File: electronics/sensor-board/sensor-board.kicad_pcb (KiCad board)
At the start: 4 copper layers, 270 x 30 mm, 196 parts, among them J1 Load Cell Input, J10 Load Cell Input, J11 FSR Input, J12 Digital Input, J13 Conn_02x04_Odd_Even, J14 Conn_02x04_Odd_Even, J15 Conn_02x04_Odd_Even, J16 Conn_02x04_Odd_Even, J17 Conn_01x06_Male, J18 USB_C_Receptacle_USB2.0, J19 Conn_02x04_Odd_Even, J2 FSR Input, J20 Barrel_Jack_MountingPin, J3 Digital Input, J4 Load Cell Input, J5 FSR Input, J6 Digital Input, J7 Load Cell Input, J8 FSR Input, J9 Digital Input, SW1 SW_DIP_x02, SW10 SW_DIP_x02, SW11 SW_DIP_x02, SW12 SW_DIP_x02, SW2 SW_DIP_x02, SW3 SW_DIP_x02, SW4 SW_DIP_x02, SW5 SW_Push, SW6 SW_Push, SW7 SW_DIP_x02, SW8 SW_DIP_x02, SW9 SW_DIP_x02, U1 LMV321, U10 TJA1042T-3, U11 74HCT245, U12 AMS1117-3.3, U13 TPS5430DDA, U2 INA826, U3 LMV321, U4 INA826, U5 LMV321, U6 INA826, U7 LMV321, U8 INA826, U9 STM32F302C8Tx, Y1 8MHz

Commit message: Remove DIP switches and re-organize CAN connectors
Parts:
- removed C51, C52, C54, C56: 100u, Capacitor_SMD:C_1210_3225Metric
- removed C53: 1u, Capacitor_SMD:C_0603_1608Metric
- removed C55: 100n, Capacitor_SMD:C_0603_1608Metric
- removed H3, H4: MountingHole_Pad, MountingHole:MountingHole_3.2mm_M3_Pad
- removed J19: Conn_02x04_Odd_Even, Connector_PinHeader_2.54mm:PinHeader_2x04_P2.54mm_Vertical
- removed J20: Barrel_Jack_MountingPin, sensor-board:BarrelJack_MP
- removed R54, R55: 5.1k, Resistor_SMD:R_0603_1608Metric
- removed R56: 1.5k, Resistor_SMD:R_0603_1608Metric
- removed R57, R58: 22R, Resistor_SMD:R_0603_1608Metric
- removed R59, R60, R61, R62, R63, R64, R65, R66, R67: 10k, Resistor_SMD:R_0603_1608Metric
- removed R68: 3.3k, Resistor_SMD:R_0603_1608Metric
- removed SW10, SW11, SW12, SW3, SW4, SW7, SW8, SW9: SW_DIP_x02, Button_Switch_THT:SW_DIP_SPSTx02_Slide_6.7x6.64mm_W7.62mm_P2.54mm_LowProfile
- removed SW5, SW6: SW_Push, sensor-board:TS-1187A-B-A-B
- C40: value 100p -> 100n
- C41: value 4.7n -> 10u; footprint Capacitor_SMD:C_0603_1608Metric -> Capacitor_SMD:C_1206_3216Metric
- C42: value 100p -> 10u; footprint Capacitor_SMD:C_0603_1608Metric -> Capacitor_SMD:C_1206_3216Metric
- C43: value 100p -> 22u; footprint Capacitor_SMD:C_0603_1608Metric -> Capacitor_SMD:C_1206_3216Metric
- C44: value 4.7n -> 100n
- C45: value 100p -> 100u; footprint Capacitor_SMD:C_0603_1608Metric -> Capacitor_SMD:C_1210_3225Metric
- C46: value 100n -> 100u; footprint Capacitor_SMD:C_0603_1608Metric -> Capacitor_SMD:C_1210_3225Metric
- C47: value 10u -> 1u; footprint Capacitor_SMD:C_1206_3216Metric -> Capacitor_SMD:C_0603_1608Metric
- C48: value 10u -> 100u; footprint Capacitor_SMD:C_1206_3216Metric -> Capacitor_SMD:C_1210_3225Metric
- C49: value 22u -> 100u; footprint Capacitor_SMD:C_1206_3216Metric -> Capacitor_SMD:C_1210_3225Metric
- J15: value Conn_02x04_Odd_Even -> Conn_01x06_Male; footprint Connector_PinHeader_2.54mm:PinHeader_2x04_P2.54mm_Vertical -> Connector_PinHeader_2.54mm:PinHeader_1x06_P2.54mm_Vertical
- J16: value Conn_02x04_Odd_Even -> USB_C_Receptacle_USB2.0; footprint Connector_PinHeader_2.54mm:PinHeader_2x04_P2.54mm_Vertical -> Connector_USB:USB_C_Receptacle_Palconn_UTC16-G
- J17: value Conn_01x06_Male -> Conn_02x04_Odd_Even; footprint Connector_PinHeader_2.54mm:PinHeader_1x06_P2.54mm_Vertical -> Connector_PinHeader_2.54mm:PinHeader_2x04_P2.54mm_Vertical
- J18: value USB_C_Receptacle_USB2.0 -> Barrel_Jack_MountingPin; footprint Connector_USB:USB_C_Receptacle_Palconn_UTC16-G -> sensor-board:BarrelJack_MP
- R34: value 10k -> 47R
- R35: value 10k -> 56R
- R36: value 10k -> 120R
- R37: value 10k -> 220R
- R38, R39: value 10k -> 5.1k
- R40: value 10k -> 1.5k
- R41: value 10k -> 22R
- R42: value 47R -> 22R
- R43: value 56R -> 10k
- R44: value 120R -> 10k
- R45: value 220R -> 10k
- R46, R47, R50, R51: value 27R -> 10k
- R48, R49, R52: value 33R -> 10k
- R53: value 33R -> 3.3k
- SW1, SW2: value SW_DIP_x02 -> SW_Push; footprint Button_Switch_THT:SW_DIP_SPSTx02_Slide_6.7x6.64mm_W7.62mm_P2.54mm_LowProfile -> sensor-board:TS-1187A-B-A-B
- moved H2 209.3 mm to (315.8, 102.6)
- moved J14 202.2 mm to (315.9, 111.2)
- moved U13 183.7 mm to (334.2, 101.0)
- moved J15 143.6 mm to (207.4, 117.0), turned to 90 degrees
- moved SW1 142.5 mm to (216.2, 126.4)
- moved U9 142.4 mm to (212.4, 138.4), turned to 45 degrees
- moved J18 136.0 mm to (304.2, 106.6), turned to -90 degrees
- moved C35 127.7 mm to (219.2, 138.4), turned to -90 degrees
- moved SW2 124.9 mm to (208.6, 126.4)
- moved C31 124.7 mm to (218.4, 130.0)
- moved C33 121.9 mm to (212.4, 145.2)
- moved C36 112.8 mm to (212.4, 131.6)
- moved C37 105.7 mm to (205.6, 138.4), turned to 90 degrees
- moved R33 103.3 mm to (206.4, 130.0), turned to 180 degrees
- moved C49 93.5 mm to (231.3, 88.3)
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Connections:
- C3 pad 2: Net-(C10-Pad2) -> Net-(C3-Pad2)
- C38 pad 1: +3.3V -> GND
- C39 pad 1: GND -> +3.3V
- C4 pad 1: Net-(C10-Pad2) -> Net-(C3-Pad2)
- C4 pad 2: Net-(C11-Pad2) -> Net-(C4-Pad2)
- C40 pad 1: Net-(C40-Pad1) -> +5V
- C41 pad 1: Net-(C40-Pad1) -> +24V
- C42 pad 1: Net-(C40-Pad1) -> +5V
- C43 pad 1: Net-(C43-Pad1) -> +3.3V
- C44 pad 1: Net-(C43-Pad1) -> Net-(C44-Pad1)
- C44 pad 2: GND -> Net-(C44-Pad2)
- C45 pad 1: Net-(C43-Pad1) -> +5V
- C47 pad 1: +24V -> +3.3VA
- C49 pad 1: +3.3V -> +5V
- C5 pad 1: Net-(C11-Pad2) -> Net-(C4-Pad2)
- C50 pad 1: Net-(C50-Pad1) -> +3.3VA
- C50 pad 2: Net-(C50-Pad2) -> GND
- D4 pad 1: Net-(C50-Pad1) -> Net-(C44-Pad1)
- J1 pad 1: Net-(J4-Pad1) -> Net-(J1-Pad1)
- J1 pad 3: /sensor_handler2/SENSE+ -> /sensor_handler1/SENSE+
- J1 pad 4: /sensor_handler2/SENSE- -> /sensor_handler1/SENSE-
- J13 pad 5: GND -> +24V
- J13 pad 6: /pad_bus/CANH -> GND
- J13 pad 8: /pad_bus/CANL -> GND
- J14 pad 2: /pad_bus/CANH -> Net-(J13-Pad2)
- J14 pad 4: /pad_bus/CANL -> Net-(J13-Pad4)
- J14 pad 5: GND -> +24V
- J14 pad 6: Net-(J14-Pad6) -> GND
- J14 pad 8: Net-(J14-Pad8) -> GND
- J15 pad 1: +24V -> +3.3V
- J15 pad 2: Net-(J14-Pad6) -> /controller/SWCLK
- J15 pad 3: +24V -> GND
- J15 pad 4: Net-(J14-Pad8) -> /controller/SWDIO
- J15 pad 5: GND -> /controller/NRST
- J15 pad 6: Net-(J15-Pad6) -> /controller/SWO
- J17 pad 1: +3.3V -> Net-(J17-Pad1)
- J17 pad 2: /controller/SWCLK -> +5V
- J17 pad 3: GND -> Net-(J17-Pad3)
- J17 pad 4: /controller/SWDIO -> +5V
- J17 pad 5: /controller/NRST -> Net-(J17-Pad5)
- J17 pad 6: /controller/SWO -> GND
- J2 pad 2: /controller/FSR_UR -> /controller/FSR_UL
- J3 pad 1: /controller/DIGITALSENSOR_UR -> /controller/DIGITALSENSOR_UL
- L1 pad 1: Net-(C50-Pad1) -> Net-(C44-Pad1)
- R1 pad 2: Net-(R10-Pad1) -> Net-(R1-Pad2)
- R2 pad 1: Net-(R10-Pad1) -> Net-(R1-Pad2)
- R3 pad 2: Net-(J4-Pad1) -> Net-(J1-Pad1)
- R33 pad 1: /controller/PANEL_POS0 -> GND
- R33 pad 2: GND -> Net-(R33-Pad2)
- R34 pad 1: /controller/PANEL_POS1 -> Net-(D1-Pad2)
- R34 pad 2: GND -> Net-(R34-Pad2)
- R35 pad 1: /controller/PANEL_POS2 -> Net-(D2-Pad2)
- R35 pad 2: GND -> Net-(R35-Pad2)
- R36 pad 1: /controller/PANEL_POS3 -> Net-(D3-Pad2)
- R36 pad 2: GND -> Net-(R36-Pad2)
- R37 pad 1: /controller/SENSOR_TYPE0 -> Net-(C30-Pad2)
- R37 pad 2: GND -> Net-(R37-Pad2)
- R38 pad 1: /controller/SENSOR_TYPE1 -> Net-(J16-PadA5)
- R39 pad 1: /controller/SENSOR_POS -> Net-(J16-PadB5)
- R4 pad 1: /controller/FSR_UR -> /controller/FSR_UL
- R40 pad 1: /controller/DEBUG -> Net-(J16-PadA7)
- R40 pad 2: GND -> +3.3V
- R41 pad 1: GND -> Net-(J16-PadA7)
- R41 pad 2: Net-(R41-Pad2) -> /controller/USBD_N
- R42 pad 1: Net-(D1-Pad2) -> Net-(J16-PadA6)
- R42 pad 2: Net-(R42-Pad2) -> /controller/USBD_P
- R43 pad 1: Net-(D2-Pad2) -> +5V
- R43 pad 2: Net-(R43-Pad2) -> /controller/LED_EN
- R44 pad 1: Net-(D3-Pad2) -> GND
- R45 pad 1: Net-(C30-Pad2) -> GND
- R46 pad 1: Net-(R46-Pad1) -> GND
- R47 pad 1: Net-(R47-Pad1) -> GND
- R48 pad 1: Net-(R46-Pad2) -> Net-(R48-Pad1)
- R48 pad 2: Net-(C40-Pad1) -> GND
- R49 pad 1: Net-(R47-Pad2) -> Net-(R49-Pad1)
- R49 pad 2: Net-(C40-Pad1) -> GND
- R5 pad 2: /controller/DIGITALSENSOR_UR -> /controller/DIGITALSENSOR_UL
- R50 pad 2: Net-(R50-Pad2) -> GND
- R51 pad 2: Net-(R51-Pad2) -> GND
- R52 pad 1: Net-(R50-Pad2) -> +5V
- R52 pad 2: Net-(C43-Pad1) -> Net-(R52-Pad2)
- R53 pad 1: Net-(R51-Pad2) -> Net-(R52-Pad2)
- R53 pad 2: Net-(C43-Pad1) -> GND
- R6 pad 1: /sensor_handler2/SENSE- -> /sensor_handler1/SENSE-
- R6 pad 2: Net-(C10-Pad2) -> Net-(C3-Pad2)
- R7 pad 1: /sensor_handler2/SENSE+ -> /sensor_handler1/SENSE+
- R7 pad 2: Net-(C11-Pad2) -> Net-(C4-Pad2)
- R8 pad 1: Net-(R16-Pad1) -> Net-(R8-Pad1)
- R8 pad 2: Net-(R16-Pad2) -> Net-(R8-Pad2)
- SW1 pad 1: +3.3V -> GND
- SW1 pad 2: +3.3V -> /controller/NRST
- SW2 pad 2: +3.3V -> Net-(R33-Pad2)
- TP1 pad 1: /controller/FSR_UR -> /controller/FSR_UL
- TP2 pad 1: /controller/DIGITALSENSOR_UR -> /controller/DIGITALSENSOR_UL
- TP3 pad 1: /controller/LOADCELL_UR -> /controller/LOADCELL_UL
- TP7 pad 1: /controller/DIGITALSENSOR_DL -> /controller/FSR_DL
- U1 pad 1: Net-(R10-Pad1) -> Net-(R1-Pad2)
- U1 pad 3: /sensor_handler2/VREF -> /sensor_handler1/VREF
- U1 pad 4: /sensor_handler2/VREF -> /sensor_handler1/VREF
- U10 pad 6: /pad_bus/CANL -> Net-(J13-Pad4)
- U10 pad 7: /pad_bus/CANH -> Net-(J13-Pad2)
- U11 pad 11: Net-(R66-Pad1) -> Net-(R51-Pad1)
- U11 pad 12: Net-(R65-Pad1) -> Net-(R50-Pad1)
- U11 pad 13: Net-(R64-Pad1) -> Net-(R49-Pad1)
- U11 pad 14: Net-(R63-Pad1) -> Net-(R48-Pad1)
- U11 pad 15: Net-(J19-Pad7) -> Net-(J17-Pad7)
- U11 pad 16: Net-(J19-Pad5) -> Net-(J17-Pad5)
- U11 pad 17: Net-(J19-Pad3) -> Net-(J17-Pad3)
- U11 pad 18: Net-(J19-Pad1) -> Net-(J17-Pad1)
- U11 pad 19: GND -> /controller/LED_EN
- U11 pad 6: Net-(R59-Pad2) -> Net-(R44-Pad2)
- U11 pad 7: Net-(R60-Pad2) -> Net-(R45-Pad2)
- U11 pad 8: Net-(R61-Pad2) -> Net-(R46-Pad2)
- U11 pad 9: Net-(R62-Pad2) -> Net-(R47-Pad2)
- U13 pad 1: Net-(C50-Pad1) -> Net-(C44-Pad1)
- U13 pad 4: Net-(R67-Pad2) -> Net-(R52-Pad2)
- U13 pad 8: Net-(C50-Pad2) -> Net-(C44-Pad2)
- U2 pad 1: Net-(C10-Pad2) -> Net-(C3-Pad2)
- U2 pad 2: Net-(R16-Pad1) -> Net-(R8-Pad1)
- U2 pad 3: Net-(R16-Pad2) -> Net-(R8-Pad2)
- U2 pad 4: Net-(C11-Pad2) -> Net-(C4-Pad2)
- U2 pad 6: /sensor_handler2/VREF -> /sensor_handler1/VREF
- U2 pad 7: /controller/LOADCELL_UR -> /controller/LOADCELL_UL
- U9 pad 2: Net-(R42-Pad2) -> Net-(R34-Pad2)
- U9 pad 22: /controller/SENSOR_POS -> /controller/LED_EN
- U9 pad 29: /controller/SENSOR_TYPE0 -> unconnected-(U9-Pad29)
- U9 pad 3: Net-(R43-Pad2) -> Net-(R35-Pad2)
- U9 pad 30: /controller/SENSOR_TYPE1 -> unconnected-(U9-Pad30)
- U9 pad 31: /controller/DEBUG -> unconnected-(U9-Pad31)
- U9 pad 4: Net-(R44-Pad2) -> Net-(R36-Pad2)
- U9 pad 40: /controller/PANEL_POS0 -> unconnected-(U9-Pad40)
- U9 pad 41: /controller/PANEL_POS1 -> unconnected-(U9-Pad41)
- U9 pad 42: /controller/PANEL_POS2 -> unconnected-(U9-Pad42)
- U9 pad 43: /controller/PANEL_POS3 -> unconnected-(U9-Pad43)
- U9 pad 44: Net-(R41-Pad2) -> Net-(R33-Pad2)
- U9 pad 6: Net-(R45-Pad2) -> Net-(R37-Pad2)
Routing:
- net /controller/LOADCELL_UL: track 0.00 -> 44.5 mm
- net /controller/LOADCELL_UR: track 51.5 -> 7.00 mm
- net /controller/DIGITALSENSOR_UR: track 59.0 -> 39.3 mm
- net /controller/DIGITALSENSOR_UL: track 0.00 -> 19.7 mm
- net GND: track 53.2 -> 69.6 mm, vias 36 -> 48
- net Net-(R33-Pad2): track 0.00 -> 15.1 mm
- net +3.3V: track 0.00 -> 13.1 mm, vias 0 -> 9
- net Net-(C4-Pad2): track 0.00 -> 13.0 mm
- net Net-(C11-Pad2): track 26.0 -> 13.0 mm
- net /controller/FSR_UR: track 59.0 -> 46.6 mm
- net /controller/FSR_UL: track 0.00 -> 12.4 mm
- net Net-(C3-Pad2): track 0.00 -> 11.0 mm
- net Net-(C10-Pad2): track 22.0 -> 11.0 mm
- net Net-(J13-Pad2): track 9.04 -> 0.00 mm
- net Net-(J15-Pad6): track 8.98 -> 0.00 mm
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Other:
- board text added: "BOOT"
- board text added: "RESET"
- board text removed: "ON"

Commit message: Further PCB layout
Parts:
- moved R46 179.0 mm to (251.8, 142.6), turned to 180 degrees
- moved R49 165.4 mm to (241.4, 142.6), turned to 180 degrees
- moved R47 159.3 mm to (251.8, 144.2), turned to 180 degrees
- moved R48 157.8 mm to (241.4, 141.0), turned to 180 degrees
- moved R44 154.7 mm to (251.8, 139.4), turned to 180 degrees
- moved R50 153.6 mm to (241.4, 144.2), turned to 180 degrees
- moved R51 153.0 mm to (241.4, 145.8), turned to 180 degrees
- moved R43 149.5 mm to (251.8, 145.8), turned to 180 degrees
- moved R45 149.4 mm to (251.8, 141.0), turned to 180 degrees
- moved C40 147.0 mm to (241.4, 139.4), turned to 180 degrees
- moved R38 138.4 mm to (231.8, 121.2), turned to -90 degrees
- moved R40 136.7 mm to (234.6, 118.4), turned to 180 degrees
- moved R42 134.6 mm to (243.2, 115.0), turned to -90 degrees
- moved R41 133.9 mm to (245.0, 115.0), turned to -90 degrees
- moved R39 116.0 mm to (228.6, 119.2), turned to 180 degrees
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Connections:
- net Net-(J16-PadA6) renamed /usb/USB_P
- net Net-(J16-PadA7) renamed /usb/USB_N
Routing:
- net GND: track 69.6 -> 82.5 mm, vias 48 -> 58
- net Net-(R47-Pad2): track 0.00 -> 9.12 mm
- net Net-(R46-Pad2): track 0.00 -> 7.79 mm
- net Net-(R33-Pad2): track 15.1 -> 7.72 mm
- net Net-(J16-PadA4): track 0.00 -> 6.80 mm
- net Net-(R45-Pad2): track 0.00 -> 6.66 mm
- net Net-(R44-Pad2): track 0.00 -> 6.38 mm
- net Net-(R48-Pad1): track 0.00 -> 5.87 mm
- net Net-(J17-Pad7): track 0.00 -> 5.47 mm
- net /usb/USB_N: track 0.00 -> 5.23 mm
- net /usb/USB_P: track 0.00 -> 5.21 mm
- net Net-(R49-Pad1): track 0.00 -> 4.46 mm
- net Net-(J17-Pad1): track 0.00 -> 4.16 mm
- net Net-(J17-Pad5): track 0.00 -> 3.93 mm
- net +5V: track 0.00 -> 3.66 mm, vias 0 -> 3
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- added copper zone on In1.Cu, net +3.3V
- added copper zone on In1.Cu, net +5V

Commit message: Upgrade to STM32G4 and CAN FD
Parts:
- removed R37: 220R, Resistor_SMD:R_0603_1608Metric
- removed R40: 1.5k, Resistor_SMD:R_0603_1608Metric
- removed R41, R42: 22R, Resistor_SMD:R_0603_1608Metric
- removed SW1, SW2: SW_Push, sensor-board:TS-1187A-B-A-B
- C32: value 100n -> 10n
- R33: value 10k -> 220R
- U9: value STM32F302C8Tx -> STM32G431CBT6
- moved C43 171.9 mm to (247.4, 136.8)
- moved R52 158.7 mm to (239.8, 138.8), turned to -90 degrees
- moved C42 153.8 mm to (243.8, 135.6), turned to 90 degrees
- moved C44 149.5 mm to (235.0, 146.6), turned to -90 degrees
- moved R53 146.7 mm to (238.2, 138.8), turned to 90 degrees
- moved C45 142.9 mm to (239.8, 135.6), turned to 180 degrees
- moved C41 142.8 mm to (227.0, 142.6), turned to 90 degrees
- moved C32 129.9 mm to (220.0, 142.4)
- moved C34 125.2 mm to (220.0, 140.8)
- moved U10 124.8 mm to (201.2, 133.8), turned to 180 degrees
- moved D1 121.4 mm to (199.0, 137.6)
- moved D3 119.3 mm to (199.0, 140.8)
- moved C30 119.0 mm to (202.2, 146.4), turned to 90 degrees
- moved C39 115.6 mm to (199.7, 130.3)
- moved Y1 114.4 mm to (199.4, 144.8), turned to 90 degrees
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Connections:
- D4 pad 1: Net-(C44-Pad1) -> Net-(C44-Pad2)
- J16 pad A6: /usb/USB_P -> /controller/USBD_P
- J16 pad A7: /usb/USB_N -> /controller/USBD_N
- J16 pad B6: /usb/USB_P -> /controller/USBD_P
- J16 pad B7: /usb/USB_N -> /controller/USBD_N
- L1 pad 1: Net-(C44-Pad1) -> Net-(C44-Pad2)
- R33 pad 1: GND -> Net-(C30-Pad2)
- U9 pad 10: /controller/LOADCELL_UL -> /controller/LOADCELL_DL
- U9 pad 11: /controller/LOADCELL_UR -> /controller/LOADCELL_DR
- U9 pad 12: /controller/LOADCELL_DL -> /controller/FSR_UL
- U9 pad 13: /controller/LOADCELL_DR -> /controller/FSR_UR
- U9 pad 14: /controller/FSR_UL -> /controller/FSR_DL
- U9 pad 15: /controller/DIGITALSENSOR_UL -> /controller/FSR_DR
- U9 pad 16: /controller/FSR_UR -> /controller/DIGITALSENSOR_UL
- U9 pad 18: /controller/FSR_DL -> /controller/DIGITALSENSOR_DL
- U9 pad 19: /controller/FSR_DR -> GND
- U9 pad 20: /controller/DIGITALSENSOR_DL -> unconnected-(U9-Pad20)
- U9 pad 21: /controller/DIGITALSENSOR_DR -> +3.3VA
- U9 pad 22: /controller/LED_EN -> /controller/DIGITALSENSOR_DR
- U9 pad 25: /controller/LED_SEG_UL -> /controller/LED_EN
- U9 pad 26: /controller/LED_SEG_UR -> /controller/LED_SEG_UL
- U9 pad 27: /controller/LED_SEG_DL -> /controller/LED_SEG_UR
- U9 pad 28: /controller/LED_SEG_DR -> /controller/LED_SEG_DL
- U9 pad 29: unconnected-(U9-Pad29) -> /controller/LED_SEG_DR
- U9 pad 32: /controller/USBD_N -> unconnected-(U9-Pad32)
- U9 pad 33: /controller/USBD_P -> /controller/USBD_N
- U9 pad 34: /controller/SWDIO -> /controller/USBD_P
- U9 pad 37: /controller/SWCLK -> /controller/SWDIO
- U9 pad 38: unconnected-(U9-Pad38) -> /controller/SWCLK
- U9 pad 39: /controller/SWO -> unconnected-(U9-Pad39)
- U9 pad 40: unconnected-(U9-Pad40) -> /controller/SWO
- U9 pad 44: Net-(R33-Pad2) -> unconnected-(U9-Pad44)
- U9 pad 6: Net-(R37-Pad2) -> Net-(R33-Pad2)
- U9 pad 8: GND -> /controller/LOADCELL_UL
- U9 pad 9: +3.3VA -> /controller/LOADCELL_UR
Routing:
- net +5V: track 3.66 -> 17.6 mm
- net Net-(C29-Pad2): track 0.00 -> 11.5 mm
- net GND: track 82.5 -> 93.2 mm, vias 58 -> 63
- net /controller/NRST: track 7.74 -> 0.04 mm
- net /controller/CAN_RX: track 0.00 -> 7.19 mm
- net Net-(R34-Pad2): track 0.00 -> 7.00 mm
- net Net-(R35-Pad2): track 0.00 -> 6.36 mm
- net Net-(R36-Pad2): track 0.00 -> 6.17 mm
- net Net-(C30-Pad2): track 0.00 -> 5.65 mm
- net Net-(R52-Pad2): track 0.00 -> 5.62 mm
- net /usb/USB_N: track 5.23 -> 0.00 mm
- net /usb/USB_P: track 5.21 -> 0.00 mm
- net /controller/CAN_TX: track 0.00 -> 4.95 mm
- net /controller/USBD_N: track 0.06 -> 4.29 mm
- net /controller/USBD_P: track 0.06 -> 4.26 mm
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- added copper zone on B.Cu, net +24V
- added copper zone on F.Cu, net +24V
- added copper zone on F.Cu, net +5V
- added copper zone on F.Cu, net GND
- added copper zone on F.Cu, net Net-(C44-Pad1)
- added copper zone on F.Cu, net Net-(C44-Pad2)
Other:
- board text removed: "BOOT"
- board text removed: "RESET"

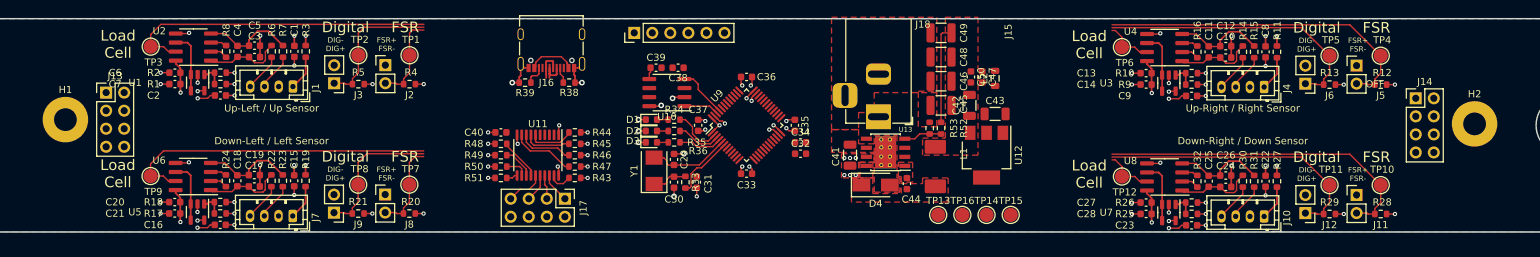
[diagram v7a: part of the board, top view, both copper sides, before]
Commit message: Switch to G4, preliminary signal layout
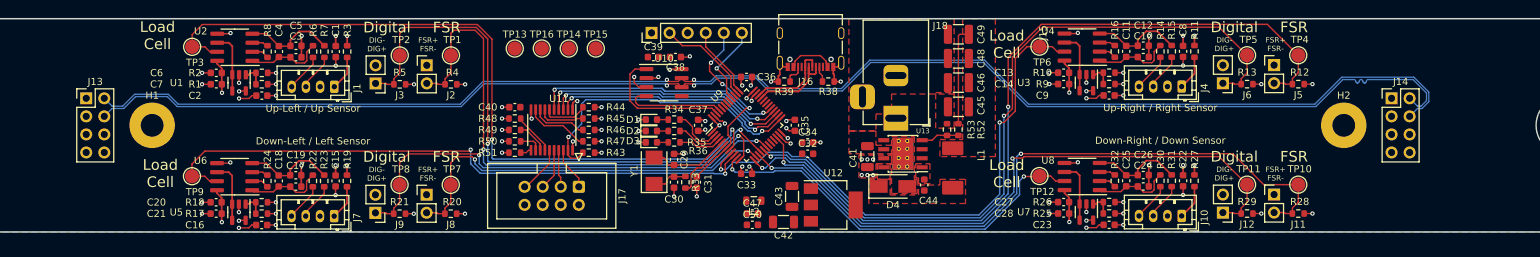
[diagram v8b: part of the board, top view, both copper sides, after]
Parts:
- J17: footprint Connector_PinHeader_2.54mm:PinHeader_2x04_P2.54mm_Vertical -> Connector_IDC:IDC-Header_2x04_P2.54mm_Vertical
- moved TP13 64.0 mm to (179.8, 127.6)
- moved TP16 63.6 mm to (183.6, 127.6)
- moved TP14 63.2 mm to (187.4, 127.6)
- moved TP15 62.9 mm to (191.2, 127.6)
- moved L2 38.0 mm to (213.4, 149.0), turned to 180 degrees
- moved C47 37.6 mm to (213.2, 150.8), turned to 0 degrees
- moved C50 37.1 mm to (213.2, 152.4), turned to 0 degrees
- moved J16 36.5 mm to (221.4, 127.7)
- moved R38 36.5 mm to (223.9, 132.2)
- moved R39 36.5 mm to (217.7, 132.2)
- moved C42 30.9 mm to (217.6, 152.0), turned to 180 degrees
- moved C43 30.8 mm to (218.8, 148.4), turned to 90 degrees
- moved U12 22.7 mm to (224.6, 149.6), turned to 0 degrees
- moved H2 18.4 mm to (296.4, 138.4)
- moved H1 12.2 mm to (128.8, 138.4)
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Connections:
- J13 pad 2: Net-(J13-Pad2) -> /pad_bus/CAN_P
- J13 pad 4: Net-(J13-Pad4) -> /pad_bus/CAN_N
- J14 pad 2: Net-(J13-Pad2) -> /pad_bus/CAN_N
- J14 pad 4: Net-(J13-Pad4) -> /pad_bus/CAN_P
- U10 pad 6: Net-(J13-Pad4) -> /pad_bus/CAN_N
- U10 pad 7: Net-(J13-Pad2) -> /pad_bus/CAN_P
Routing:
- net /pad_bus/CAN_P: track 0.00 -> 202.8 mm, vias 0 -> 2
- net /pad_bus/CAN_N: track 0.00 -> 202.7 mm, vias 0 -> 2
- net /controller/LOADCELL_UR: track 7.00 -> 76.3 mm, vias 0 -> 2
- net /controller/FSR_UR: track 46.6 -> 112.8 mm, vias 0 -> 2
- net /controller/DIGITALSENSOR_UR: track 39.3 -> 102.5 mm, vias 0 -> 2
- net /controller/DIGITALSENSOR_UL: track 19.7 -> 82.8 mm, vias 0 -> 2
- net /controller/FSR_UL: track 12.4 -> 74.6 mm, vias 0 -> 2
- net /controller/LOADCELL_UL: track 44.5 -> 105.0 mm, vias 0 -> 2
- net /controller/LOADCELL_DR: track 7.00 -> 56.8 mm, vias 0 -> 2
- net /controller/FSR_DR: track 46.6 -> 96.2 mm, vias 0 -> 2
- net /controller/DIGITALSENSOR_DR: track 39.3 -> 88.4 mm, vias 0 -> 2
- net /controller/DIGITALSENSOR_DL: track 19.9 -> 65.7 mm, vias 0 -> 2
- net /controller/FSR_DL: track 12.5 -> 56.1 mm, vias 0 -> 2
- net /controller/LOADCELL_DL: track 44.7 -> 87.1 mm, vias 0 -> 2
- net /controller/LED_EN: track 3.31 -> 42.1 mm, vias 0 -> 2
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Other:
- board text removed: "OFF"
